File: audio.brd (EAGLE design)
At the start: 40.6 x 48.6 mm, 49 parts, among them IC1 OPA1664, IC2 OPA1662

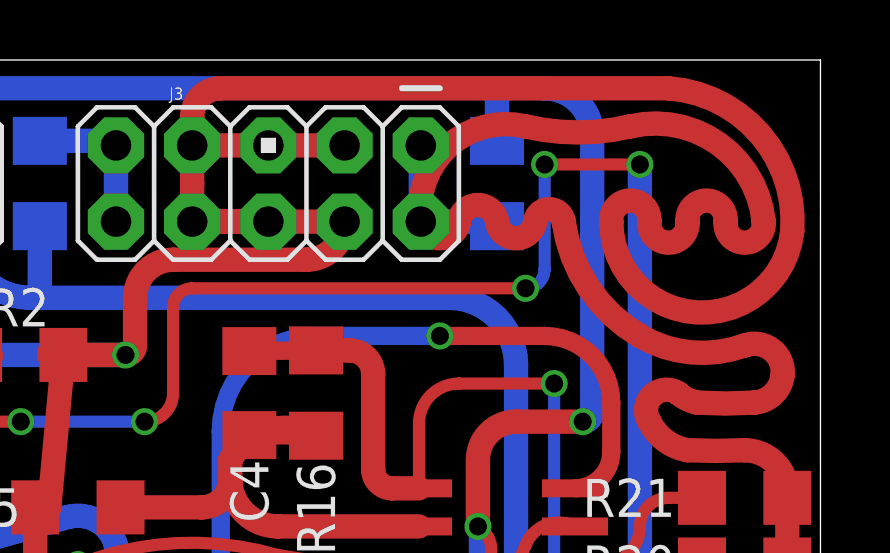
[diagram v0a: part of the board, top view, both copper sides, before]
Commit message: removed dumb mistake on audio board image and .brd file
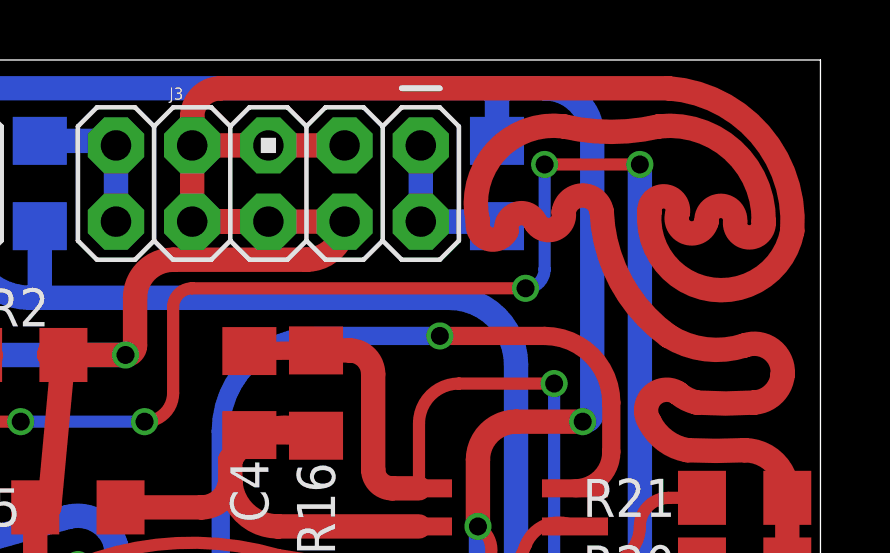
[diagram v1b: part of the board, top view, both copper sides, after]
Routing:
- net GND: track 236.8 -> 231.6 mm
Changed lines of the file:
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@@
 <wire x1="20.6375" y1="47.625" x2="35.56" y2="47.625" width="0.8128" layer="1"/>
 <wire x1="35.56" y1="47.625" x2="39.6875" y2="42.8625" width="0.8128" layer="1" curve="-90"/>
-<wire x1="39.6875" y1="42.8625" x2="33.655" y2="43.18" width="0.8128" layer="1" curve="-174.27519"/>
-<wire x1="33.655" y1="43.18" x2="34.925" y2="43.18" width="0.8128" layer="1" curve="-191.449326"/>
-<wire x1="34.925" y1="43.18" x2="36.195" y2="43.18" width="0.8128" layer="1" curve="191.449103"/>
-<wire x1="36.195" y1="43.18" x2="37.465" y2="43.18" width="0.8128" layer="1" curve="-191.448545"/>
-<wire x1="37.465" y1="43.18" x2="38.735" y2="43.18" width="0.8128" layer="1" curve="191.448545"/>
-<wire x1="38.735" y1="43.18" x2="34.29" y2="46.355" width="0.8128" layer="1" curve="97.476087"/>
-<wire x1="34.29" y1="46.355" x2="30.7975" y2="46.355" width="0.8128" layer="1" curve="-26.400705"/>
-<wire x1="30.7975" y1="46.355" x2="27.305" y2="43.18" width="0.8128" layer="1" curve="110.948175"/>
-<wire x1="27.305" y1="43.18" x2="28.575" y2="43.18" width="0.8128" layer="1" curve="164.504599"/>
-<wire x1="28.575" y1="43.18" x2="29.845" y2="43.18" width="0.8128" layer="1" curve="-164.504599"/>
-<wire x1="29.845" y1="43.18" x2="31.115" y2="43.18" width="0.8128" layer="1" curve="164.504599"/>
-<wire x1="31.115" y1="43.18" x2="32.0675" y2="43.18" width="0.8128" layer="1" curve="-164.50423"/>
-<wire x1="32.0675" y1="43.18" x2="34.6075" y2="39.37" width="0.8128" layer="1" curve="51.885119"/>
-<wire x1="34.6075" y1="39.37" x2="38.1" y2="39.0525" width="0.8128" layer="1" curve="50.345868"/>
+<wire x1="39.6875" y1="42.8625" x2="34.925" y2="43.4975" width="0.8128" layer="1" curve="-174.27519"/>
+<wire x1="34.925" y1="43.4975" x2="35.8775" y2="43.4975" width="0.8128" layer="1" curve="-191.449326"/>
+<wire x1="35.8775" y1="43.4975" x2="36.83" y2="43.18" width="0.8128" layer="1" curve="191.449103"/>
+<wire x1="36.83" y1="43.18" x2="37.7825" y2="43.18" width="0.8128" layer="1" curve="-191.448545"/>
+<wire x1="37.7825" y1="43.18" x2="38.735" y2="43.18" width="0.8128" layer="1" curve="191.448545"/>
+<wire x1="38.735" y1="43.18" x2="35.2425" y2="46.355" width="0.8128" layer="1" curve="97.476087"/>
+<wire x1="35.2425" y1="46.355" x2="32.0675" y2="46.355" width="0.8128" layer="1" curve="-26.400705"/>
+<wire x1="32.0675" y1="46.355" x2="29.21" y2="43.18" width="0.8128" layer="1" curve="110.948175"/>
+<wire x1="29.21" y1="43.18" x2="30.1625" y2="42.8625" width="0.8128" layer="1" curve="164.504599"/>
+<wire x1="30.1625" y1="42.8625" x2="31.115" y2="43.18" width="0.8128" layer="1" curve="-164.504599"/>
+<wire x1="31.115" y1="43.18" x2="32.0675" y2="43.4975" width="0.8128" layer="1" curve="164.504599"/>
+<wire x1="32.0675" y1="43.4975" x2="33.3375" y2="43.4975" width="0.8128" layer="1" curve="-164.50423"/>
+<wire x1="33.3375" y1="43.4975" x2="35.56" y2="39.37" width="0.8128" layer="1" curve="51.885119"/>
+<wire x1="35.56" y1="39.37" x2="38.1" y2="39.0525" width="0.8128" layer="1" curve="50.345868"/>
 <wire x1="38.1" y1="39.0525" x2="39.37" y2="38.1" width="0.8128" layer="1" curve="-113.696632"/>
 <wire x1="39.37" y1="38.1" x2="38.4175" y2="37.1475" width="0.8128" layer="1" curve="-82.563748"/>
@@
 <wire x1="24.765" y1="45.72" x2="22.225" y2="45.72" width="0.8128" layer="1"/>
 <wire x1="19.685" y1="45.72" x2="22.225" y2="45.72" width="0.8128" layer="1"/>
-<wire x1="19.685" y1="43.18" x2="19.685" y2="44.45" width="0.8128" layer="1"/>
-<wire x1="19.685" y1="44.45" x2="19.685" y2="45.72" width="0.8128" layer="1"/>
+<wire x1="19.685" y1="43.18" x2="19.685" y2="45.72" width="0.8128" layer="1"/>
 <wire x1="19.685" y1="43.18" x2="22.225" y2="43.18" width="0.8128" layer="1"/>
 <wire x1="19.685" y1="43.18" x2="24.765" y2="43.18" width="0.8128" layer="1"/>
